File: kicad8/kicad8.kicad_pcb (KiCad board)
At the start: 2 copper layers, 192 parts, among them J1 USB_C_Receptacle_USB2.0, U1 STM32F072CBT6, U2 PRTR5V0U2X, U3 XC6206PxxxMR-Regulator_Linear

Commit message: Changed: switch footprint
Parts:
- removed MX15: MX_SW_HS, MX_Hotswap:MX-Hotswap-1U
- added SW1: RotaryEncoder_Switch, Rotary_Encoder:RotaryEncoder_Alps_EC11E-Switch_Vertical_H20mm, F.Cu at (315.5, 24.7)
- MX1, MX10, MX11, MX12, MX13, MX14, MX16, MX17, MX18, MX19, MX2, MX20, MX21, MX22, MX23, MX24, MX25, MX26, MX27, MX28, MX29, MX3, MX30, MX31, MX32, MX33, MX34, MX35, MX36, MX37, MX38, MX39, MX4, MX40, MX41, MX42, MX43, MX44, MX45, MX46, MX47, MX48, MX49, MX5, MX50, MX51, MX52, MX53, MX54, MX55, MX56, MX57, MX58, MX59, MX6, MX60, MX61, MX62, MX63, MX64, MX65, MX66, MX67, MX68, MX69, MX7, MX70, MX71, MX72, MX73, MX74, MX75, MX76, MX77, MX78, MX79, MX8, MX80, MX81, MX82, MX83, MX84, MX9: footprint MX_Hotswap:MX-Hotswap-1U -> PCM_marbastlib-mx:SW_MX_HS_CPG151101S11_1u
- moved D15 16.2 mm to (296.3, 24.7), turned to 0 degrees
- moved C1 10.6 mm to (351.5, 49.5)
- moved C7 10.6 mm to (351.5, 48.2)
- moved BOOT1 10.6 mm to (346.9, 58.7)
- moved C10 10.6 mm to (347.2, 34.0)
- moved C2 10.6 mm to (344.4, 34.2)
- moved C3 10.6 mm to (345.7, 37.2)
- moved C4 10.6 mm to (354.4, 37.5)
- moved C5 10.6 mm to (345.4, 46.0)
- moved C6 10.6 mm to (345.9, 47.5)
- moved C8 10.6 mm to (346.9, 27.2)
- moved C9 10.6 mm to (348.4, 30.5)
- moved F1 10.6 mm to (349.9, 28.2)
- moved J1 10.6 mm to (349.9, 16.0)
- moved R1 10.6 mm to (346.9, 25.2)
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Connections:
- MX78 pad 1: col3 -> col6
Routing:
- net col9: track 0.00 -> 119.7 mm
- net col11: track 0.00 -> 119.7 mm
- net col10: track 0.00 -> 119.7 mm
- net col2: track 0.00 -> 114.9 mm
- net col1: track 0.00 -> 112.9 mm
- net col6: track 0.00 -> 112.8 mm
- net col13: track 0.00 -> 111.8 mm
- net col12: track 0.00 -> 111.8 mm
- net col0: track 0.00 -> 105.1 mm
- net col14: track 0.00 -> 101.3 mm
- net col8: track 0.00 -> 94.8 mm
- net col7: track 0.00 -> 94.8 mm
- net col3: track 0.00 -> 92.8 mm
- net col5: track 0.00 -> 92.8 mm
- net col4: track 0.00 -> 92.8 mm
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
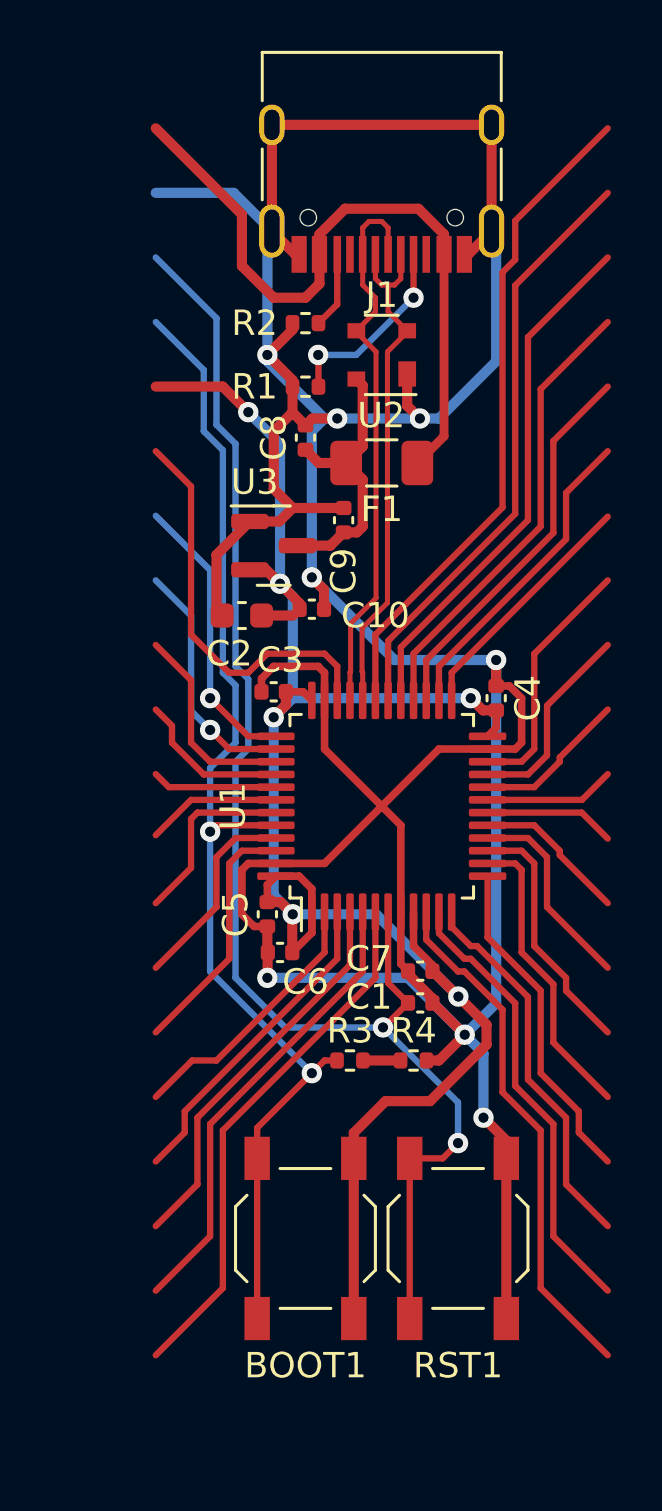
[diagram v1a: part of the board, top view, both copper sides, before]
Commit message: Removed: traces from the template
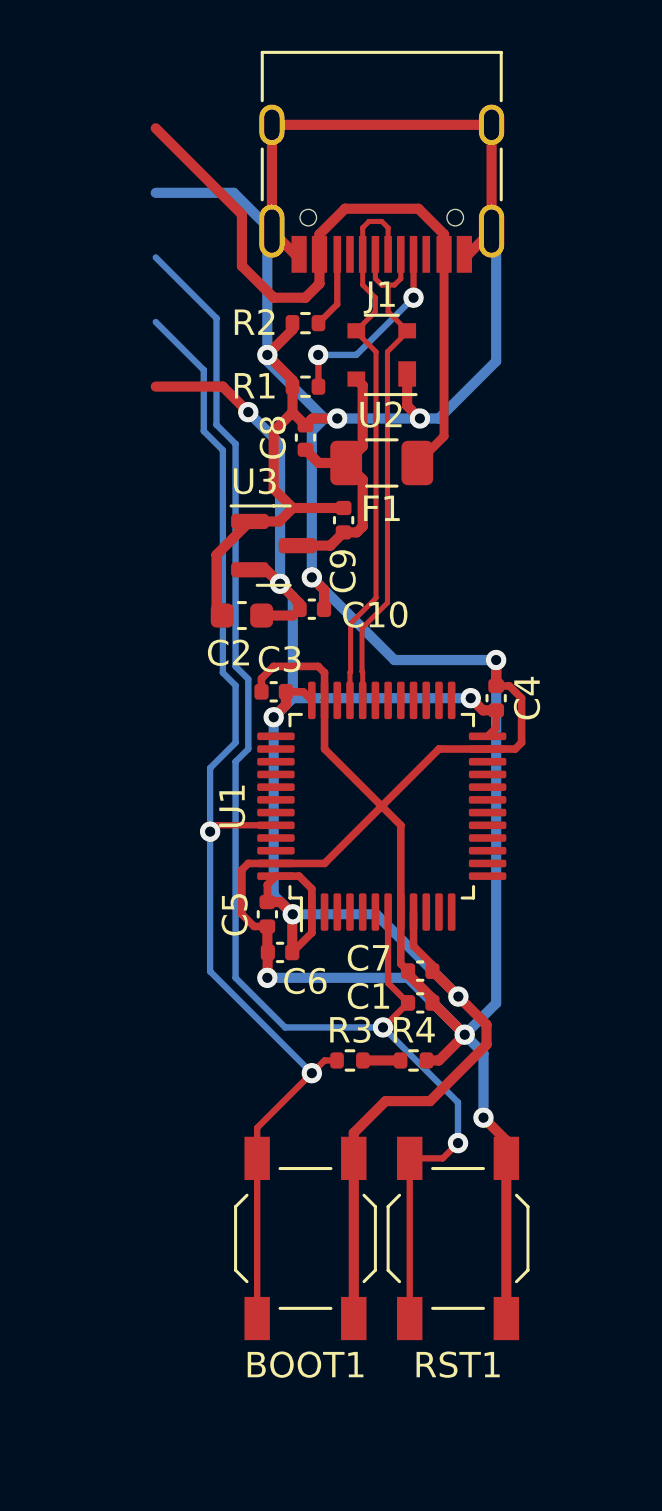
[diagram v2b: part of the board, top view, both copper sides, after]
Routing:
- net /A10: track 26.3 -> 0.00 mm
- net /A9: track 23.5 -> 0.00 mm
- net /F1: track 21.0 -> 0.00 mm
- net /A8: track 20.8 -> 0.00 mm
- net /A0: track 20.5 -> 0.00 mm
- net /F0: track 18.3 -> 0.00 mm
- net /B15: track 18.0 -> 0.00 mm
- net /A1: track 17.8 -> 0.00 mm
- net /A13: track 16.0 -> 0.00 mm
- net /C15: track 15.5 -> 0.00 mm
- net /B14: track 15.3 -> 0.00 mm
- net /A2: track 14.5 -> 0.00 mm
- net /A3: track 13.2 -> 0.00 mm
- net /C14: track 12.8 -> 0.00 mm
- net /B13: track 12.6 -> 0.00 mm
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
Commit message: Changed: Switch matrix layout
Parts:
- J1: footprint Connector_USB:USB_C_Receptacle_HRO_TYPE-C-31-M-12 -> PCM_marbastlib-various:USB_C_Receptacle_HRO_TYPE-C-31-M-12
- SW1: footprint Rotary_Encoder:RotaryEncoder_Alps_EC11E-Switch_Vertical_H20mm -> PCM_marbastlib-various:ROT_Alps_EC11E-Switch
- moved BOOT1 129.0 mm to (471.4, 92.6), turned to 0 degrees
- moved C6 123.2 mm to (460.2, 93.6), turned to -90 degrees
- moved C5 123.1 mm to (458.7, 94.1), turned to 0 degrees
- moved R3 122.2 mm to (464.4, 90.9), turned to 90 degrees
- moved RST1 121.7 mm to (471.4, 86.6), turned to 180 degrees
- moved C2 119.2 mm to (446.9, 95.1), turned to -90 degrees
- moved R4 119.0 mm to (464.4, 88.4), turned to 90 degrees
- moved C3 118.6 mm to (449.9, 93.9), turned to -90 degrees
- moved C1 117.3 mm to (462.2, 88.1), turned to 90 degrees
- moved U3 116.6 mm to (444.2, 93.9), turned to 90 degrees
- moved C7 116.5 mm to (460.9, 88.1), turned to -90 degrees
- moved C10 115.4 mm to (446.7, 92.4), turned to 90 degrees
- moved U1 114.9 mm to (454.4, 89.6), turned to 180 degrees
- moved C8 113.7 mm to (439.9, 92.6), turned to 180 degrees
- moved R1 113.2 mm to (437.9, 92.6), turned to 90 degrees
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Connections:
- MX73 pad 1: col13 -> col14
- MX74 pad 1: col14 -> col13
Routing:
- net row0: track 269.2 -> 283.2 mm
- net row4: track 283.4 -> 296.8 mm
- net row2: track 281.0 -> 290.5 mm
- net row1: track 285.8 -> 295.3 mm
- net row3: track 278.6 -> 288.1 mm
- net row5: track 283.4 -> 290.8 mm
- net col12: track 111.8 -> 118.6 mm
- net col13: track 111.8 -> 118.6 mm
- net col14: track 101.3 -> 108.0 mm
- net (no net): track 0.00 -> 1.92 mm

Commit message: Added: col and row traces
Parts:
- moved D15 0.56 mm to (309.1, 28.2)
- moved D13 0.08 mm to (263.7, 23.4)
- moved D14 0.08 mm to (287.6, 23.4)
- moved D29 0.08 mm to (282.8, 47.2)
- moved D43 0.08 mm to (263.7, 66.3)
- moved D44 0.08 mm to (287.6, 66.3)
- moved D72 0.08 mm to (266.1, 104.4)
- moved D82 0.08 mm to (278.0, 128.2)
- moved D17 0.08 mm to (44.7, 47.2)
- moved D46 0.08 mm to (32.8, 85.3)
- moved D1 0.08 mm to (25.6, 23.4)
- moved D16 0.08 mm to (25.6, 47.2)
- moved D31 0.08 mm to (30.4, 66.3)
- moved D10 0.08 mm to (206.6, 23.4)
- moved D11 0.08 mm to (225.6, 23.4)
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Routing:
- net Net-(D82-A): track 4.49 -> 0.00 mm
- net Net-(D72-A): track 4.49 -> 0.00 mm
- net Net-(D41-A): track 4.49 -> 0.00 mm
- net Net-(D38-A): track 4.49 -> 0.00 mm
- net Net-(D36-A): track 4.49 -> 0.00 mm
- net Net-(D26-A): track 4.49 -> 0.00 mm
- net Net-(D24-A): track 4.49 -> 0.00 mm
- net Net-(D8-A): track 4.49 -> 0.00 mm
- net Net-(D7-A): track 4.49 -> 0.00 mm
- net Net-(D11-A): track 4.49 -> 0.00 mm
- net Net-(D71-A): track 4.49 -> 0.00 mm
- net Net-(D69-A): track 4.49 -> 0.00 mm
- net Net-(D66-A): track 4.49 -> 0.00 mm
- net Net-(D57-A): track 4.49 -> 0.00 mm
- net Net-(D54-A): track 4.49 -> 0.00 mm
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
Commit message: Added: wiring to the switch matrix
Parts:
- BOOT1, C1, C10, C2, C3, C4, C5, C6, C7, C8, C9, F1, J1, R1, R2, R3, R4, RST1, U1, U2, U3: moved to B.Cu
- moved BOOT1 311.5 mm to (161.2, 120.1), turned to 180 degrees
- moved RST1 311.4 mm to (161.2, 113.9), turned to 0 degrees
- moved R4 297.6 mm to (168.1, 115.8)
- moved R3 297.6 mm to (168.1, 118.3)
- moved C1 292.9 mm to (170.5, 115.4)
- moved C7 157.8 mm to (303.1, 85.4), turned to 45 degrees
- moved C4 157.1 mm to (293.1, 79.6), turned to 135 degrees
- moved U1 155.2 mm to (299.5, 79.6), turned to 135 degrees
- moved C10 155.0 mm to (302.3, 35.8), turned to 180 degrees
- moved C6 154.2 mm to (306.5, 80.8), turned to 45 degrees
- moved C9 153.7 mm to (301.2, 32.4), turned to 90 degrees
- moved C5 153.6 mm to (305.7, 79.4), turned to -45 degrees
- moved F1 153.3 mm to (299.7, 30.0), turned to 0 degrees
- moved U3 152.8 mm to (303.8, 33.4), turned to 180 degrees
- moved C3 152.0 mm to (299.3, 73.4), turned to 45 degrees
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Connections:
- U1 pad 14: /A4 -> col14
- U1 pad 15: /A5 -> col13
- U1 pad 16: /A6 -> col12
- U1 pad 17: /A7 -> col11
- U1 pad 18: /B0 -> col10
- U1 pad 19: /B1 -> col9
- U1 pad 20: /B2 -> col8
- U1 pad 21: /B10 -> col7
- U1 pad 25: /B12 -> col6
- U1 pad 26: /B13 -> col5
- U1 pad 27: /B14 -> col4
- U1 pad 28: /B15 -> col3
- U1 pad 29: /A8 -> col2
- U1 pad 30: /A9 -> col1
- U1 pad 31: /A10 -> col0
- U1 pad 37: /A14 -> row2
- U1 pad 38: /A15 -> row1
- U1 pad 39: /B3 -> row0
- U1 pad 41: /B5 -> row5
- U1 pad 42: /B6 -> row4
- U1 pad 43: /B7 -> row3
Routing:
- net col3: track 92.8 -> 374.3 mm
- net col0: track 104.9 -> 383.8 mm
- net col1: track 112.8 -> 364.9 mm
- net col2: track 114.8 -> 347.3 mm
- net GND: track 162.5 -> 383.8 mm
- net +3V3: track 78.1 -> 281.2 mm
- net col4: track 92.8 -> 286.0 mm
- net col5: track 92.8 -> 266.4 mm
- net col6: track 112.8 -> 266.8 mm
- net BOOT0: track 47.3 -> 197.7 mm
- net col7: track 94.8 -> 241.7 mm
- net NRST: track 56.2 -> 191.4 mm, vias 2 -> 4
- net col8: track 94.8 -> 222.9 mm
- net col9: track 119.7 -> 229.0 mm
- net row0: track 283.1 -> 374.2 mm, vias 0 -> 2
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
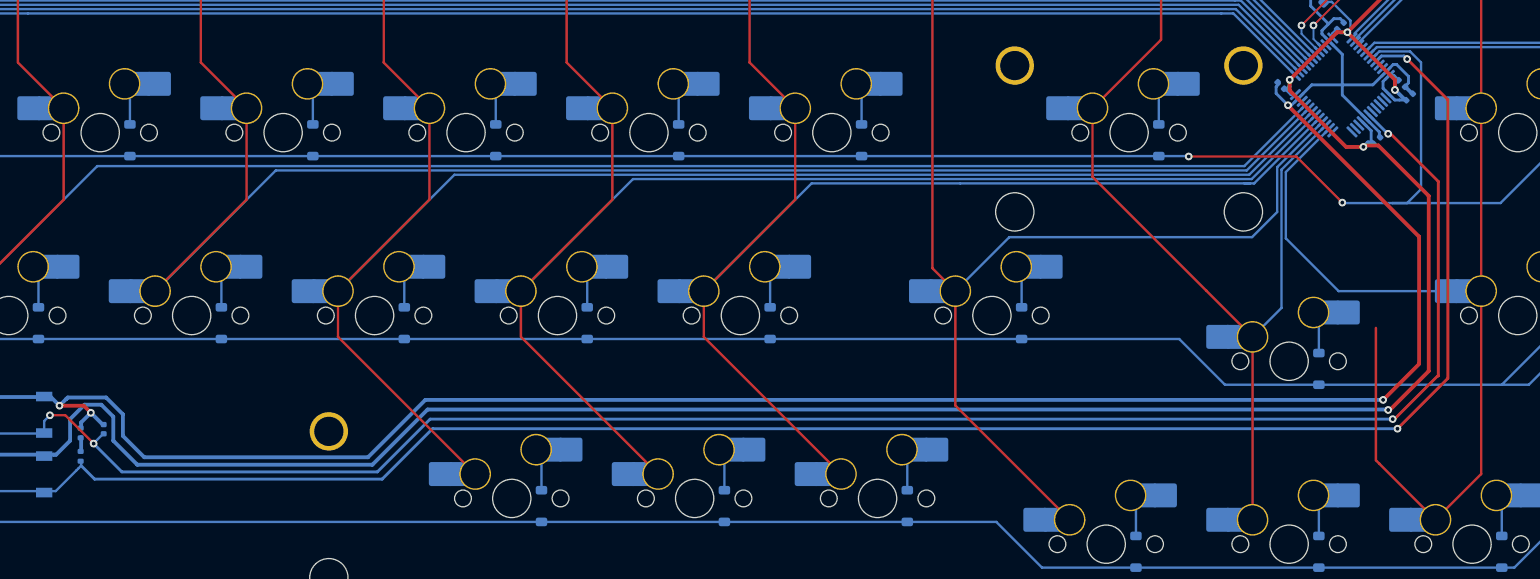
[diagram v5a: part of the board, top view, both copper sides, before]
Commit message: Removed: old project version
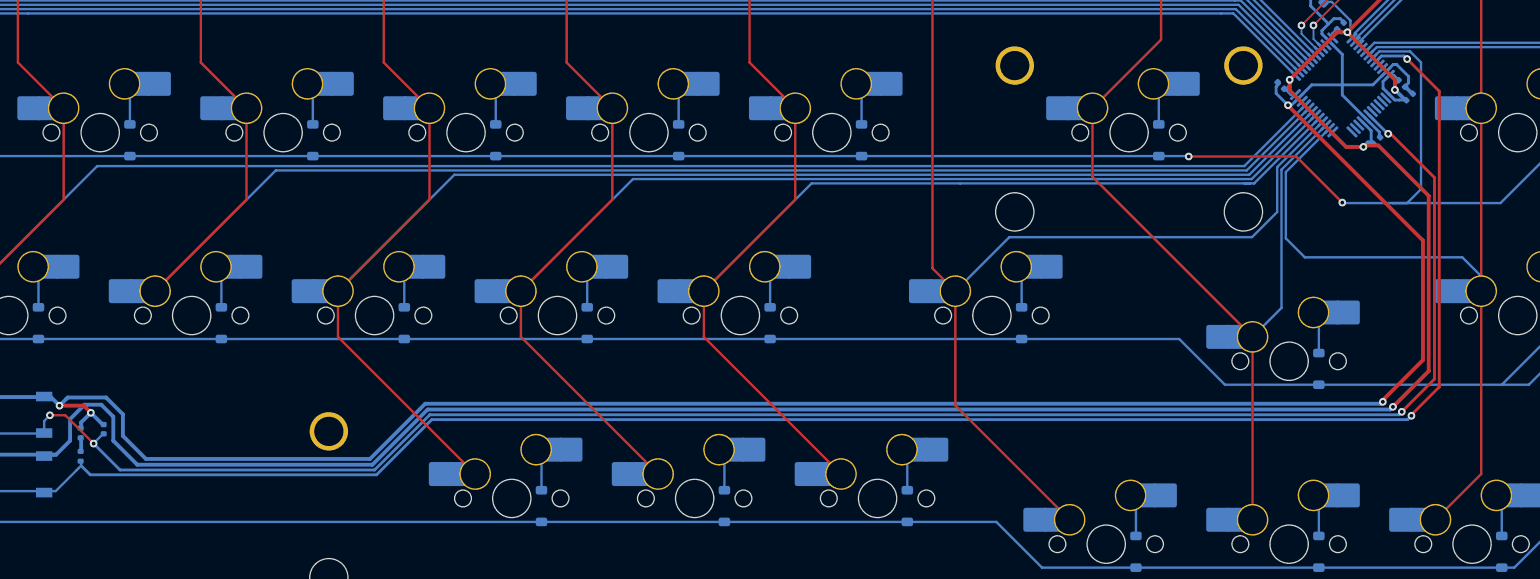
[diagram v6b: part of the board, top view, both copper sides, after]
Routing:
- net col14: track 166.5 -> 144.9 mm
- net BOOT0: track 197.7 -> 196.6 mm
- net GND: track 383.8 -> 384.4 mm
- net NRST: track 191.4 -> 190.8 mm

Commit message: Fixed: all clearance violations
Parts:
- moved BOOT1 7.07 mm to (163.2, 126.9)
- moved C1 7.07 mm to (172.5, 122.2)
- moved R4 7.07 mm to (170.1, 122.6)
- moved RST1 7.07 mm to (163.2, 120.7)
- moved R3 7.07 mm to (170.1, 125.0)
- moved D15 3.14 mm to (310.9, 30.8)
- moved D13 3.02 mm to (265.9, 25.6)
- moved D14 3.02 mm to (289.7, 25.6)
- moved D43 3.02 mm to (265.9, 68.4)
- moved D44 3.02 mm to (289.7, 68.4)
- moved D22 3.02 mm to (142.1, 49.4)
- moved D27 3.02 mm to (237.3, 49.4)
- moved D39 3.02 mm to (189.7, 68.4)
- moved D55 3.02 mm to (213.5, 87.5)
- moved D67 3.02 mm to (165.9, 106.5)
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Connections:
- U1 pad 2: /C13 -> rot1
- U1 pad 3: /C14 -> rot0
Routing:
- net rot0: track 0.00 -> 71.6 mm, vias 0 -> 1
- net rot1: track 0.00 -> 62.4 mm, vias 0 -> 1
- net Net-(D15-A): track 3.09 -> 19.5 mm
- net GND: track 384.4 -> 368.6 mm
- net BOOT0: track 196.6 -> 202.4 mm, vias 2 -> 6
- net +3V3: track 281.2 -> 278.6 mm
- net col14: track 144.9 -> 143.0 mm
- net NRST: track 190.8 -> 189.4 mm
- net row2: track 313.2 -> 314.5 mm
- net row0: track 374.2 -> 374.7 mm
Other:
- board outline added: 314.5 x 124 mm

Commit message: Finished: base keybaord
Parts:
- moved C8 2.57 mm to (304.9, 28.8)
- moved C9 2.57 mm to (303.3, 31.9)
- moved F1 2.57 mm to (301.9, 29.6)
- moved R2 2.57 mm to (304.9, 24.2)
- moved U2 2.57 mm to (301.9, 25.5)
- moved C10 2.57 mm to (304.5, 35.4)
- moved J1 2.57 mm to (301.9, 17.5)
- moved R1 2.57 mm to (304.9, 26.6)
- moved U3 2.57 mm to (305.9, 33.0)
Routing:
- net row0: track 374.7 -> 378.9 mm
- net D-: track 59.2 -> 61.7 mm
- net D+: track 61.0 -> 63.5 mm
- net +3V3: track 278.6 -> 281.2 mm
- net GND: track 368.6 -> 371.1 mm
